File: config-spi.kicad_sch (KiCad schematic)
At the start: 39 parts, among them J1 0878311420, Q7 BSS138APW, Q8 BSS138APW, U15 XC7K160T-FFG676, U3 S25FL128SAGNFI000

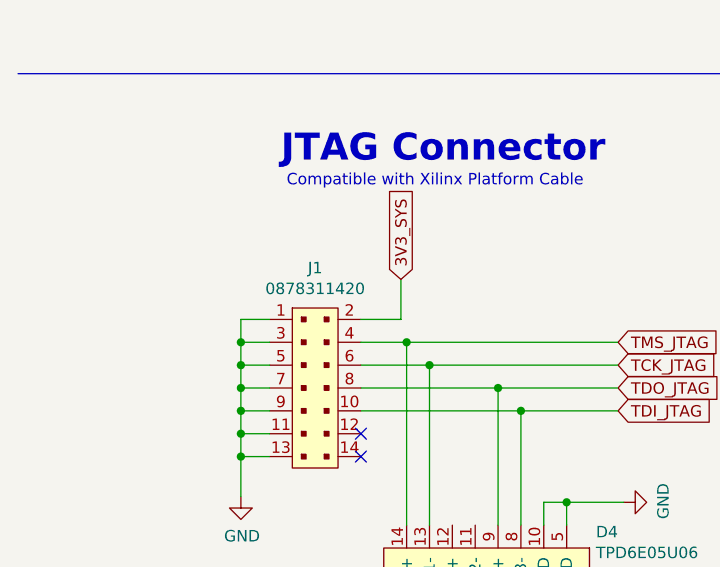
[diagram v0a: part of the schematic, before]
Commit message: Reconnect FMC signals to new socket, and JTAG to new connector
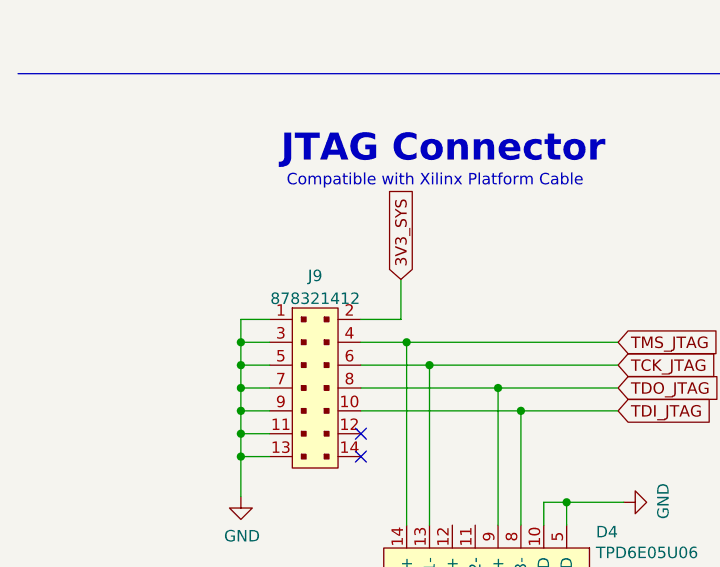
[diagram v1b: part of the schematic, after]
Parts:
- removed J1: 0878311420, data-center-dram-tester-footprints:PinHeader_2x7_P2mm_Drill1mm, symbol data-center-dram-tester:0878311420
- added J9: 878321412, antmicro-footprints:PinHeader_2x7_P2mm_SMD_no_locator, symbol antmicroRectangularConnectorsHeadersMalePins:878321412
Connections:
- net 3V3_SYS: now also J9.2
- net GND: now also J9.1, J9.11, J9.13, J9.3, J9.5, J9.7, J9.9
- net TCK_JTAG: now also J9.6
- net TDI_JTAG: now also J9.10
- net TDO_JTAG: now also J9.8
- net TMS_JTAG: now also J9.4

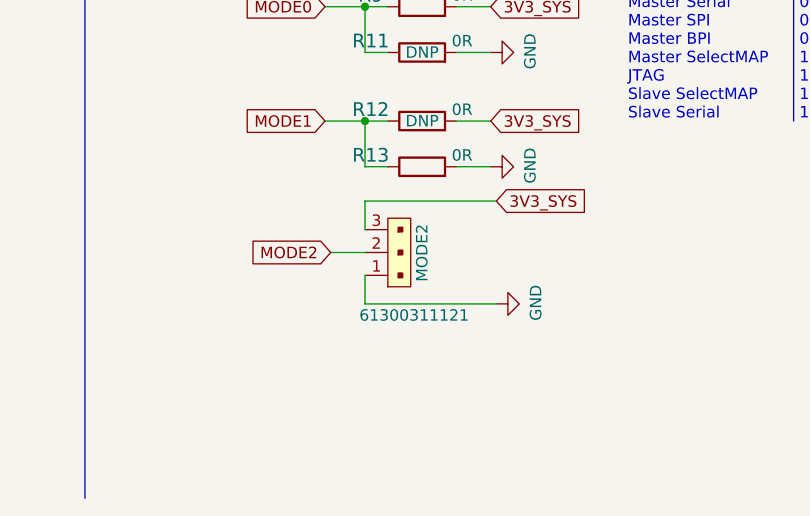
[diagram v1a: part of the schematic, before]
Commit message: Replace MODE2 jumpers with SMD DIP switch. Replace power cycle,VTT_CNTL and SLP_S4 ccircuits with tri-state buffer ones. Add possibilty to swith ETH paths with FPGA
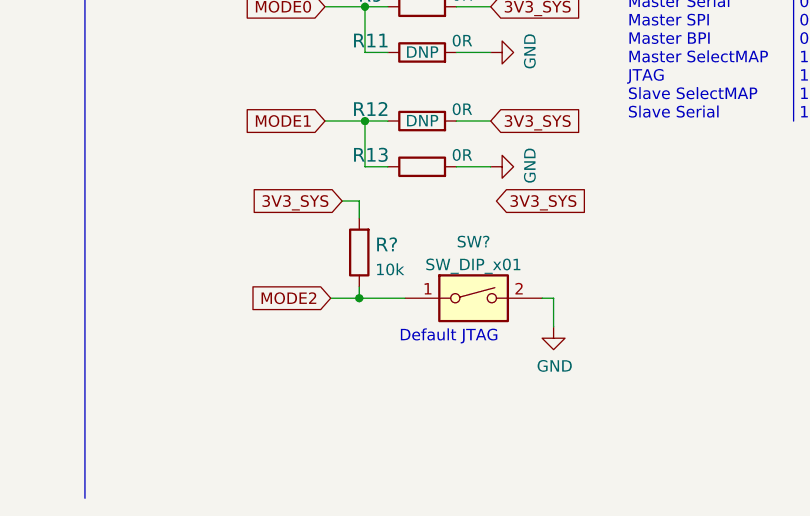
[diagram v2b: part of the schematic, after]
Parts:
- removed MODE2: 61300311121, data-center-dram-tester-footprints:PinHeader_1x3_P2.54_Drill1.1mm, symbol data-center-dram-tester:61300311121
- added R?: R_10k_0402, antmicro-footprints:0402-res, symbol antmicroResistors0402:R_10k_0402
- added SW?: SW_DIP_x01, symbol Switch:SW_DIP_x01
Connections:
- net 3V3_SYS: now also R?.2
- net GND: now also SW?.2
- net MODE2: now also R?.1, SW?.1
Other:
- note added: "Default JTAG"
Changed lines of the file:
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@@
   (junction (at 247.015 106.045) (diameter 0) (color 0 0 0 0)
   )
+  (junction (at 226.06 262.89) (diameter 0) (color 0 0 0 0)
+  )
   (junction (at 247.015 127) (diameter 0) (color 0 0 0 0)
   )
@@
     (stroke (width 0) (type default) (color 0 0 0 0))
   )
+  (wire (pts (xy 226.06 262.89) (xy 231.14 262.89))
+    (stroke (width 0) (type default) (color 0 0 0 0))
+  )
   (polyline (pts (xy 299.72 252.73) (xy 299.72 200.025))
     (stroke (width 0) (type default) (color 0 0 0 0))
@@
     (stroke (width 0) (type default) (color 0 0 0 0))
   )
+  (wire (pts (xy 247.65 266.065) (xy 247.65 262.89))
+    (stroke (width 0) (type default) (color 0 0 0 0))
+  )
+  (wire (pts (xy 247.65 262.89) (xy 246.38 262.89))
+    (stroke (width 0) (type default) (color 0 0 0 0))
+  )
   (wire (pts (xy 170.18 265.43) (xy 144.78 265.43))
     (stroke (width 0) (type default) (color 0 0 0 0))
@@
     (stroke (width 0) (type default) (color 0 0 0 0))
   )
-  (wire (pts (xy 226.695 260.35) (xy 226.695 263.525))
-    (stroke (width 0) (type default) (color 0 0 0 0))
-  )
   (wire (pts (xy 106.045 110.49) (xy 111.76 110.49))
     (stroke (width 0) (type default) (color 0 0 0 0))
@@
     (stroke (width 0) (type default) (color 0 0 0 0))
   )
-  (wire (pts (xy 226.695 263.525) (xy 241.3 263.525))
-    (stroke (width 0) (type default) (color 0 0 0 0))
-  )
   (wire (pts (xy 236.855 243.205) (xy 240.665 243.205))
     (stroke (width 0) (type default) (color 0 0 0 0))
   )
-  (wire (pts (xy 222.885 257.81) (xy 226.695 257.81))
-    (stroke (width 0) (type default) (color 0 0 0 0))
-  )
   (wire (pts (xy 130.175 105.41) (xy 155.575 105.41))
     (stroke (width 0) (type default) (color 0 0 0 0))
@@
     (stroke (width 0) (type default) (color 0 0 0 0))
   )
+  (wire (pts (xy 224.155 252.095) (xy 226.06 252.095))
+    (stroke (width 0) (type default) (color 0 0 0 0))
+  )
   (wire (pts (xy 135.89 80.01) (xy 135.89 86.995))
     (stroke (width 0) (type default) (color 0 0 0 0))
@@
     (stroke (width 0) (type default) (color 0 0 0 0))
   )
-  (wire (pts (xy 226.695 252.095) (xy 241.3 252.095))
-    (stroke (width 0) (type default) (color 0 0 0 0))
-  )
   (wire (pts (xy 135.89 110.49) (xy 135.89 94.615))
     (stroke (width 0) (type default) (color 0 0 0 0))
@@
     (stroke (width 0) (type default) (color 0 0 0 0))
   )
-  (wire (pts (xy 226.695 255.27) (xy 226.695 252.095))
-    (stroke (width 0) (type default) (color 0 0 0 0))
-  )
   (wire (pts (xy 36.83 240.03) (xy 36.83 242.57))
     (stroke (width 0) (type default) (color 0 0 0 0))
@@
     (stroke (width 0) (type default) (color 0 0 0 0))
   )
+  (wire (pts (xy 222.885 262.89) (xy 226.06 262.89))
+    (stroke (width 0) (type default) (color 0 0 0 0))
+  )
   (wire (pts (xy 106.045 118.11) (xy 111.76 118.11))
     (stroke (width 0) (type default) (color 0 0 0 0))
@@
     (stroke (width 0) (type default) (color 0 0 0 0))
   )
+  (wire (pts (xy 226.06 261.62) (xy 226.06 262.89))
+    (stroke (width 0) (type default) (color 0 0 0 0))
+  )
   (wire (pts (xy 135.89 110.49) (xy 119.38 110.49))
     (stroke (width 0) (type default) (color 0 0 0 0))
@@
     (stroke (width 0) (type default) (color 0 0 0 0))
   )
+  (wire (pts (xy 226.06 252.095) (xy 226.06 254))
+    (stroke (width 0) (type default) (color 0 0 0 0))
+  )
   (wire (pts (xy 154.94 110.49) (xy 135.89 110.49))
     (stroke (width 0) (type default) (color 0 0 0 0))
@@
     (effects (font (size 1.27 1.27)) (justify left bottom))
   )
+  (text "Default JTAG" (at 230.505 267.97 0)
+    (effects (font (size 1.27 1.27)) (justify left bottom))
+  )
   (text "FPGA BANK 0" (at 303.53 48.895 0)
     (effects (font (size 2.9972 2.9972) (thickness 0.5994) bold) (justify left bottom))
@@
     )
   )
-  (global_label "MODE2" (shape input) (at 222.885 257.81 180) (fields_autoplaced)
-    (effects (font (size 1.27 1.27)) (justify right))
-    (property "Intersheet References" "${INTERSHEET_REFS}" (id 0) (at 0 0 0)
-      (effects (font (size 1.27 1.27)) hide)
-    )
-  )
   (global_label "TMS_JTAG" (shape input) (at 78.74 229.87 0) (fields_autoplaced)
     (effects (font (size 1.27 1.27)) (justify left))
@@
     )
   )
+  (global_label "MODE2" (shape input) (at 222.885 262.89 180) (fields_autoplaced)
+    (effects (font (size 1.27 1.27)) (justify right))
+    (property "Intersheet References" "${INTERSHEET_REFS}" (id 0) (at 0 5.08 0)
+      (effects (font (size 1.27 1.27)) hide)
+    )
+  )
+  (global_label "3V3_SYS" (shape input) (at 224.155 252.095 180) (fields_autoplaced)
+    (effects (font (size 1.27 1.27)) (justify right))
+    (property "Intersheet References" "${INTERSHEET_REFS}" (id 0) (at 465.455 504.19 0)
+      (effects (font (size 1.27 1.27)) hide)
+    )
+  )
   (global_label "EMCCLK" (shape input) (at 384.175 229.235 0) (fields_autoplaced)
     (effects (font (size 1.27 1.27)) (justify left))
@@
     (pin "2")
   )
-  (symbol (lib_id "data-center-dram-tester:GND") (at 241.3 263.525 90) (unit 1)
+  (symbol (lib_id "data-center-dram-tester:GND") (at 247.65 266.065 0) (unit 1)
     (in_bom yes) (on_board yes)
-    (property "Reference" "#PWR04" (id 0) (at 247.65 263.525 0)
+    (property "Reference" "#PWR04" (id 0) (at 247.65 272.415 0)
       (effects (font (size 1.27 1.27)) hide)
     )
-    (property "Value" "GND" (id 1) (at 245.6942 263.398 0))
-    (property "Footprint" "" (id 2) (at 241.3 263.525 0)
+    (property "Value" "GND" (id 1) (at 247.777 270.4592 0))
+    (property "Footprint" "" (id 2) (at 247.65 266.065 0)
       (effects (font (size 1.27 1.27)) hide)
     )
-    (property "Datasheet" "" (id 3) (at 241.3 263.525 0)
+    (property "Datasheet" "" (id 3) (at 247.65 266.065 0)
       (effects (font (size 1.27 1.27)) hide)
     )
@@
     (pin "1")
   )
-  (symbol (lib_id "data-center-dram-tester:61300311121") (at 230.505 260.35 90) (unit 1)
-    (in_bom yes) (on_board yes)
-    (property "Reference" "MODE2" (id 0) (at 233.045 254.635 0)
-      (effects (font (size 1.27 1.27)) (justify right))
-    )
-    (property "Value" "61300311121" (id 1) (at 226.06 264.795 90)
-      (effects (font (size 1.27 1.27)) (justify right))
-    )
-    (property "Footprint" "data-center-dram-tester-footprints:PinHeader_1x3_P2.54_Drill1.1mm" (id 2) (at 225.425 255.27 0)
-      (effects (font (size 1.524 1.524)) (justify left) hide)
-    )
-    (property "Datasheet" "https://katalog.we-online.de/em/datasheet/6130xx11121.pdf" (id 3) (at 222.885 255.27 0)
-      (effects (font (size 1.524 1.524)) (justify left) hide)
-    )
-    (property "MPN" "61300311121" (id 4) (at 217.805 255.27 0)
-      (effects (font (size 1.524 1.524)) (justify left) hide)
-    )
-    (property "Manufacturer" "Wurth Electronics Inc." (id 5) (at 202.565 255.27 0)
-      (effects (font (size 1.524 1.524)) (justify left) hide)
-    )
-    (pin "1")
-    (pin "2")
-    (pin "3")
-  )
   (symbol (lib_id "data-center-dram-tester:C_100n_0402_6V3") (at 58.42 101.6 0) (mirror y) (unit 1)
     (in_bom yes) (on_board yes)
@@
     (pin "1")
   )
+  (symbol (lib_id "Switch:SW_DIP_x01") (at 238.76 262.89 0) (unit 1)
+    (in_bom yes) (on_board yes) (fields_autoplaced)
+    (property "Reference" "SW?" (id 0) (at 238.76 256.6502 0))
+    (property "Value" "SW_DIP_x01" (id 1) (at 238.76 259.1871 0))
+    (property "Footprint" "" (id 2) (at 238.76 262.89 0)
+      (effects (font (size 1.27 1.27)) hide)
+    )
+    (property "Datasheet" "~" (id 3) (at 238.76 262.89 0)
+      (effects (font (size 1.27 1.27)) hide)
+    )
+    (pin "1")
+    (pin "2")
+  )
   (symbol (lib_id "antmicroRectangularConnectorsHeadersMalePins:878321412") (at 45.085 234.95 0) (unit 1)
     (in_bom yes) (on_board yes) (fields_autoplaced)
@@
     (pin "9")
   )
+  (symbol (lib_id "antmicroResistors0402:R_10k_0402") (at 226.06 257.81 90) (unit 1)
+    (in_bom yes) (on_board yes) (fields_autoplaced)
+    (property "Reference" "R?" (id 0) (at 227.838 256.9754 90)
+      (effects (font (size 1.524 1.524)) (justify right))
+    )
+    (property "Value" "R_10k_0402" (id 1) (at 229.87 257.81 0)
+      (effects (font (size 1.524 1.524)) hide)
+    )
+    (property "Footprint" "antmicro-footprints:0402-res" (id 2) (at 220.98 252.73 0)
+      (effects (font (size 1.524 1.524)) (justify left) hide)
+    )
+    (property "Datasheet" "" (id 3) (at 226.06 257.81 0)
+      (effects (font (size 1.27 1.27)) hide)
+    )
+    (property "Manufacturer" "VISHAY" (id 4) (at 215.9 252.73 0)
+      (effects (font (size 1.524 1.524)) (justify left) hide)
+    )
+    (property "MPN" "CRCW040210K0FKEDHP" (id 5) (at 218.44 252.73 0)
+      (effects (font (size 1.524 1.524)) (justify left) hide)
+    )
+    (property "Val" "10k" (id 6) (at 227.838 259.7405 90)
+      (effects (font (size 1.27 1.27)) (justify right))
+    )
+    (pin "1")
+    (pin "2")
+  )
 )

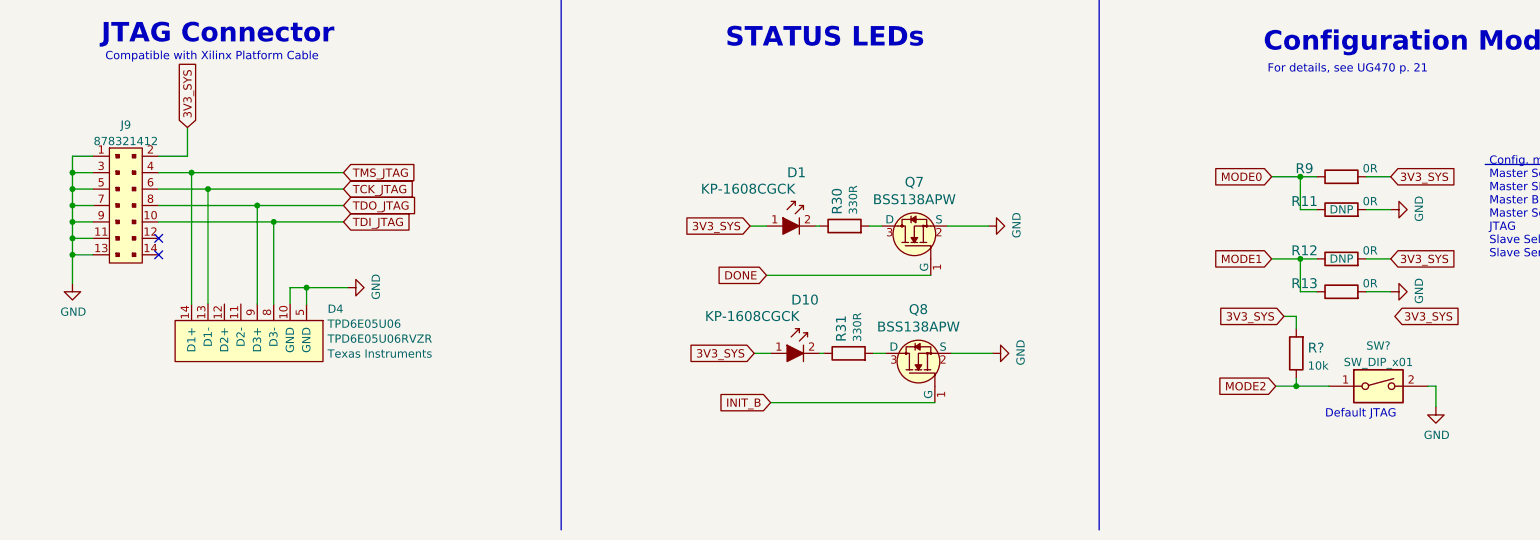
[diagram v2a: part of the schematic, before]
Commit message: Correct PCIe pin assigment, replace MODE2 symbol, export changes to PCB, progess in the new components placement
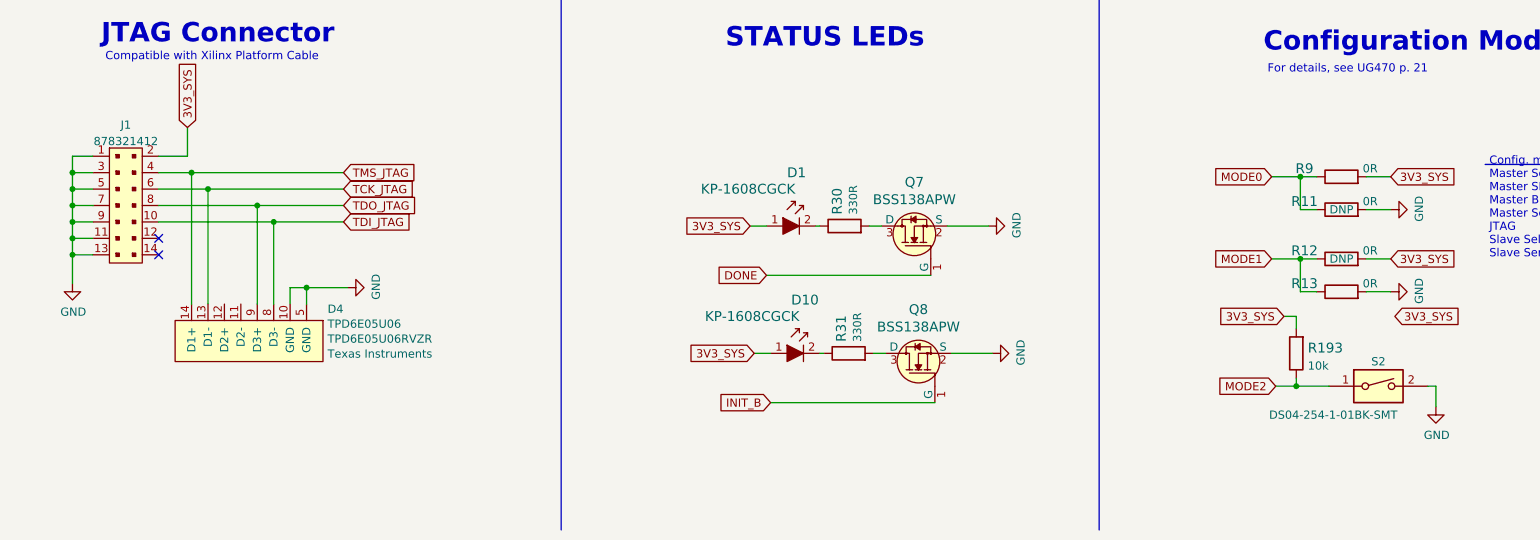
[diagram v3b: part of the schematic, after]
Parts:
- removed SW?: SW_DIP_x01, symbol Switch:SW_DIP_x01
- added S2: DS04-254-1-01BK-SMT, antmicro-footprints:SW_DS04-254-1-01BK-SMT, symbol antmicroSlideSwitches:DS04-254-1-01BK-SMT
- gave numbers to parts that had none: 1
- renumbered J9 to J1
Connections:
- net GND: now also S2.2
- net MODE2: now also S2.1
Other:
- note removed: "Default JTAG"
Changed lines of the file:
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@@
-    (effects (font (size 1.27 1.27)) (justify left bottom))
-  )
-  (text "Default JTAG" (at 230.505 267.97 0)
     (effects (font (size 1.27 1.27)) (justify left bottom))
   )
@@
     (pin "1")
   )
-  (symbol (lib_id "Switch:SW_DIP_x01") (at 238.76 262.89 0) (unit 1)
-    (in_bom yes) (on_board yes) (fields_autoplaced)
-    (property "Reference" "SW?" (id 0) (at 238.76 256.6502 0))
-    (property "Value" "SW_DIP_x01" (id 1) (at 238.76 259.1871 0))
-    (property "Footprint" "" (id 2) (at 238.76 262.89 0)
-      (effects (font (size 1.27 1.27)) hide)
-    )
-    (property "Datasheet" "~" (id 3) (at 238.76 262.89 0)
-      (effects (font (size 1.27 1.27)) hide)
-    )
-    (pin "1")
-    (pin "2")
-  )
   (symbol (lib_id "antmicroRectangularConnectorsHeadersMalePins:878321412") (at 45.085 234.95 0) (unit 1)
     (in_bom yes) (on_board yes) (fields_autoplaced)
-    (property "Reference" "J9" (id 0) (at 45.085 222.4872 0))
+    (property "Reference" "J1" (id 0) (at 45.085 222.4872 0))
     (property "Value" "878321412" (id 1) (at 45.085 225.0241 0))
     (property "Footprint" "antmicro-footprints:PinHeader_2x7_P2mm_SMD_no_locator" (id 2) (at 50.165 229.87 0)
@@
   (symbol (lib_id "antmicroResistors0402:R_10k_0402") (at 226.06 257.81 90) (unit 1)
     (in_bom yes) (on_board yes) (fields_autoplaced)
-    (property "Reference" "R?" (id 0) (at 227.838 256.9754 90)
+    (property "Reference" "R193" (id 0) (at 227.838 256.9754 90)
       (effects (font (size 1.524 1.524)) (justify right))
     )
@@
     )
     (pin "1")
+    (pin "2")
+  )
+  (symbol (lib_id "antmicroSlideSwitches:DS04-254-1-01BK-SMT") (at 238.76 262.89 0) (unit 1)
+    (in_bom yes) (on_board yes)
+    (property "Reference" "S2" (id 0) (at 238.76 259.08 0))
+    (property "Value" "DS04-254-1-01BK-SMT" (id 1) (at 231.775 267.335 0))
+    (property "Footprint" "antmicro-footprints:SW_DS04-254-1-01BK-SMT" (id 2) (at 252.73 276.86 0)
+      (effects (font (size 1.27 1.27)) hide)
+    )
+    (property "Datasheet" "https://www.mouser.pl/datasheet/2/670/ds04_254_smt-1777718.pdf" (id 3) (at 262.89 274.32 0)
+      (effects (font (size 1.27 1.27)) hide)
+    )
+    (property "MPN" "DS04-254-1-01BK-SMT" (id 4) (at 240.03 271.78 0)
+      (effects (font (size 1.27 1.27)) hide)
+    )
+    (property "Manufacturer" "CUI Devices" (id 5) (at 232.41 269.24 0)
+      (effects (font (size 1.27 1.27)) hide)
+    )
+    (pin "1")

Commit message: Update FPGA symbol (die to pad length), initial fanout for die [1..4]
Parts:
- U15: footprint data-center-dram-tester-footprints:BGA676C100P26X26_2700X2700X254 -> antmicro-footprints:xc7k160tfbg676
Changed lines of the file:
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@@
       (effects (font (size 1.27 1.27)) (justify right))
     )
-    (property "Footprint" "data-center-dram-tester-footprints:BGA676C100P26X26_2700X2700X254" (id 2) (at 365.252 118.9736 0)
+    (property "Footprint" "antmicro-footprints:xc7k160tfbg676" (id 2) (at 365.252 118.9736 0)
       (effects (font (size 1.27 1.27)) (justify right) hide)
     )
